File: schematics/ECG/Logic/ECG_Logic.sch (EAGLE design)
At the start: 77 parts, among them IC1 ADS1293, IC2 LIS3DH, IC3 MCP1703, IC4 CC2541, IC5 FSA4157, IC6 FSA4157, IC7 FSA4157, IC8 BALUN_2450BM_SERIES_SMD, X1 XTAL-2SMD, X2 XTAL_403, X3 ECS-40-20-4VX

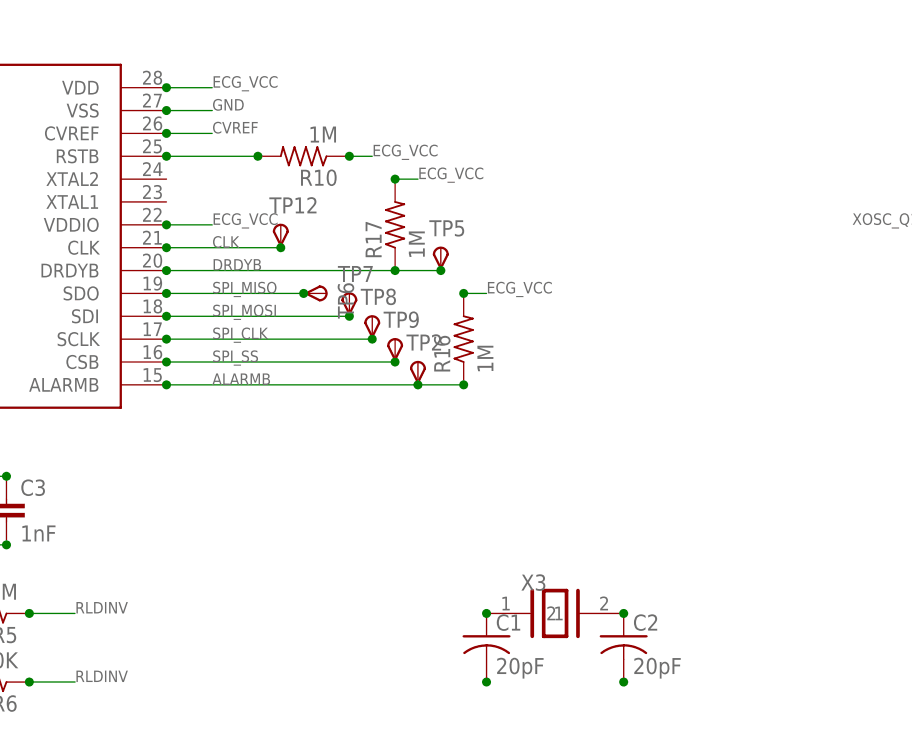
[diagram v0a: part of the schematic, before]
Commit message: expanded board size for new low profile crystal. Moved ecg input targets for shorter trace lengths to ADS1293
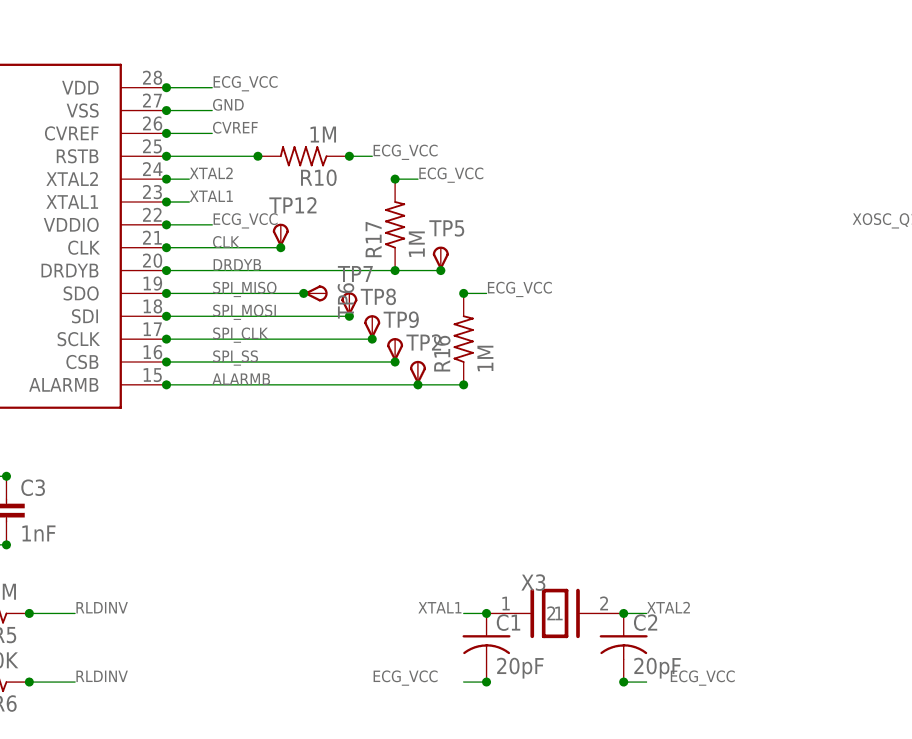
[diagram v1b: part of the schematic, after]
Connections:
- removed net N$1: C1.1, X3.1
- removed net N$10: C1.2
- removed net N$2: C2.1, X3.2
- removed net N$7: C2.2
- new net XTAL1: C1.1, IC1.XTAL1, X3.1
- new net XTAL2: C2.1, IC1.XTAL2, X3.2
- net ECG_VCC: now also C1.2, C2.2
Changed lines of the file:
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@@
 <grid distance="0.1" unitdist="inch" unit="inch" style="lines" multiple="1" display="no" altdistance="0.01" altunitdist="inch" altunit="inch"/>
 <layers>
-<layer number="1" name="Top" color="4" fill="1" visible="yes" active="no"/>
-<layer number="2" name="Route2" color="1" fill="3" visible="yes" active="no"/>
-<layer number="3" name="Route3" color="4" fill="3" visible="yes" active="no"/>
-<layer number="4" name="Route4" color="1" fill="4" visible="yes" active="no"/>
-<layer number="5" name="Route5" color="4" fill="4" visible="yes" active="no"/>
-<layer number="6" name="Route6" color="1" fill="8" visible="yes" active="no"/>
-<layer number="7" name="Route7" color="4" fill="8" visible="yes" active="no"/>
-<layer number="8" name="Route8" color="1" fill="2" visible="yes" active="no"/>
-<layer number="9" name="Route9" color="4" fill="2" visible="yes" active="no"/>
-<layer number="10" name="Route10" color="1" fill="7" visible="yes" active="no"/>
-<layer number="11" name="Route11" color="4" fill="7" visible="yes" active="no"/>
-<layer number="12" name="Route12" color="1" fill="5" visible="yes" active="no"/>
-<layer number="13" name="Route13" color="4" fill="5" visible="yes" active="no"/>
-<layer number="14" name="Route14" color="1" fill="6" visible="yes" active="no"/>
-<layer number="15" name="Route15" color="4" fill="6" visible="yes" active="no"/>
-<layer number="16" name="Bottom" color="1" fill="1" visible="yes" active="no"/>
-<layer number="17" name="Pads" color="2" fill="1" visible="yes" active="no"/>
-<layer number="18" name="Vias" color="2" fill="1" visible="yes" active="no"/>
-<layer number="19" name="Unrouted" color="6" fill="1" visible="yes" active="no"/>
-<layer number="20" name="Dimension" color="15" fill="1" visible="yes" active="no"/>
-<layer number="21" name="tPlace" color="7" fill="1" visible="yes" active="no"/>
-<layer number="22" name="bPlace" color="7" fill="1" visible="yes" active="no"/>
-<layer number="23" name="tOrigins" color="15" fill="1" visible="yes" active="no"/>
-<layer number="24" name="bOrigins" color="15" fill="1" visible="yes" active="no"/>
-<layer number="25" name="tNames" color="7" fill="1" visible="yes" active="no"/>
-<layer number="26" name="bNames" color="7" fill="1" visible="yes" active="no"/>
-<layer number="27" name="tValues" color="7" fill="1" visible="yes" active="no"/>
-<layer number="28" name="bValues" color="7" fill="1" visible="yes" active="no"/>
+<layer number="1" name="Top" color="4" fill="1" visible="no" active="no"/>
+<layer number="2" name="Route2" color="1" fill="3" visible="no" active="no"/>
+<layer number="3" name="Route3" color="4" fill="3" visible="no" active="no"/>
+<layer number="4" name="Route4" color="1" fill="4" visible="no" active="no"/>
+<layer number="5" name="Route5" color="4" fill="4" visible="no" active="no"/>
+<layer number="6" name="Route6" color="1" fill="8" visible="no" active="no"/>
+<layer number="7" name="Route7" color="4" fill="8" visible="no" active="no"/>
+<layer number="8" name="Route8" color="1" fill="2" visible="no" active="no"/>
+<layer number="9" name="Route9" color="4" fill="2" visible="no" active="no"/>
+<layer number="10" name="Route10" color="1" fill="7" visible="no" active="no"/>
+<layer number="11" name="Route11" color="4" fill="7" visible="no" active="no"/>
+<layer number="12" name="Route12" color="1" fill="5" visible="no" active="no"/>
+<layer number="13" name="Route13" color="4" fill="5" visible="no" active="no"/>
+<layer number="14" name="Route14" color="1" fill="6" visible="no" active="no"/>
+<layer number="15" name="Route15" color="4" fill="6" visible="no" active="no"/>
+<layer number="16" name="Bottom" color="1" fill="1" visible="no" active="no"/>
+<layer number="17" name="Pads" color="2" fill="1" visible="no" active="no"/>
+<layer number="18" name="Vias" color="2" fill="1" visible="no" active="no"/>
+<layer number="19" name="Unrouted" color="6" fill="1" visible="no" active="no"/>
+<layer number="20" name="Dimension" color="15" fill="1" visible="no" active="no"/>
+<layer number="21" name="tPlace" color="7" fill="1" visible="no" active="no"/>
+<layer number="22" name="bPlace" color="7" fill="1" visible="no" active="no"/>
+<layer number="23" name="tOrigins" color="15" fill="1" visible="no" active="no"/>
+<layer number="24" name="bOrigins" color="15" fill="1" visible="no" active="no"/>
+<layer number="25" name="tNames" color="7" fill="1" visible="no" active="no"/>
+<layer number="26" name="bNames" color="7" fill="1" visible="no" active="no"/>
+<layer number="27" name="tValues" color="7" fill="1" visible="no" active="no"/>
+<layer number="28" name="bValues" color="7" fill="1" visible="no" active="no"/>
 <layer number="29" name="tStop" color="7" fill="3" visible="no" active="no"/>
 <layer number="30" name="bStop" color="7" fill="6" visible="no" active="no"/>
@@
 <layer number="35" name="tGlue" color="7" fill="4" visible="no" active="no"/>
 <layer number="36" name="bGlue" color="7" fill="5" visible="no" active="no"/>
-<layer number="37" name="tTest" color="7" fill="1" visible="yes" active="no"/>
-<layer number="38" name="bTest" color="7" fill="1" visible="yes" active="no"/>
+<layer number="37" name="tTest" color="7" fill="1" visible="no" active="no"/>
+<layer number="38" name="bTest" color="7" fill="1" visible="no" active="no"/>
 <layer number="39" name="tKeepout" color="4" fill="11" visible="no" active="no"/>
 <layer number="40" name="bKeepout" color="1" fill="11" visible="no" active="no"/>
@@
 <layer number="44" name="Drills" color="7" fill="1" visible="no" active="no"/>
 <layer number="45" name="Holes" color="7" fill="1" visible="no" active="no"/>
-<layer number="46" name="Milling" color="3" fill="1" visible="yes" active="no"/>
-<layer number="47" name="Measures" color="7" fill="1" visible="yes" active="no"/>
-<layer number="48" name="Document" color="7" fill="1" visible="yes" active="no"/>
-<layer number="49" name="Reference" color="7" fill="1" visible="yes" active="no"/>
-<layer number="50" name="dxf" color="7" fill="1" visible="yes" active="no"/>
-<layer number="51" name="tDocu" color="7" fill="1" visible="yes" active="no"/>
-<layer number="52" name="bDocu" color="7" fill="1" visible="yes" active="no"/>
-<layer number="53" name="tGND_GNDA" color="7" fill="9" visible="yes" active="no"/>
-<layer number="54" name="bGND_GNDA" color="1" fill="9" visible="yes" active="no"/>
-<layer number="56" name="wert" color="7" fill="1" visible="yes" active="no"/>
+<layer number="46" name="Milling" color="3" fill="1" visible="no" active="no"/>
+<layer number="47" name="Measures" color="7" fill="1" visible="no" active="no"/>
+<layer number="48" name="Document" color="7" fill="1" visible="no" active="no"/>
+<layer number="49" name="Reference" color="7" fill="1" visible="no" active="no"/>
+<layer number="50" name="dxf" color="7" fill="1" visible="no" active="no"/>
+<layer number="51" name="tDocu" color="7" fill="1" visible="no" active="no"/>
+<layer number="52" name="bDocu" color="7" fill="1" visible="no" active="no"/>
+<layer number="53" name="tGND_GNDA" color="7" fill="9" visible="no" active="no"/>
+<layer number="54" name="bGND_GNDA" color="1" fill="9" visible="no" active="no"/>
+<layer number="56" name="wert" color="7" fill="1" visible="no" active="no"/>
 <layer number="91" name="Nets" color="2" fill="1" visible="yes" active="yes"/>
 <layer number="92" name="Busses" color="1" fill="1" visible="yes" active="yes"/>
@@
 <label x="114.3" y="66.04" size="1.27" layer="95"/>
 </segment>
+<segment>
+<pinref part="C1" gate="G$1" pin="2"/>
+<junction x="127" y="7.62"/>
+<wire x1="127" y1="7.62" x2="124.46" y2="7.62" width="0.1524" layer="91"/>
+<label x="114.3" y="7.62" size="1.27" layer="95"/>
+</segment>
+<segment>
+<pinref part="C2" gate="G$1" pin="2"/>
+<junction x="142.24" y="7.62"/>
+<wire x1="142.24" y1="7.62" x2="144.78" y2="7.62" width="0.1524" layer="91"/>
+<label x="147.32" y="7.62" size="1.27" layer="95"/>
+</segment>
 </net>
 <net name="BLUE_LED" class="0">
@@
 </segment>
 </net>
-<net name="N$1" class="0">
+<net name="XTAL1" class="0">
+<segment>
+<pinref part="IC1" gate="IC" pin="XTAL1"/>
+<wire x1="91.44" y1="60.96" x2="93.98" y2="60.96" width="0.1524" layer="91"/>
+<junction x="91.44" y="60.96"/>
+<label x="93.98" y="60.96" size="1.27" layer="95"/>
+</segment>
 <segment>
 <pinref part="X3" gate="XTAL" pin="1"/>
 <pinref part="C1" gate="G$1" pin="1"/>
 <junction x="127" y="15.24"/>
-</segment>
-</net>
-<net name="N$2" class="0">
+<wire x1="127" y1="15.24" x2="124.46" y2="15.24" width="0.1524" layer="91"/>
+<label x="119.38" y="15.24" size="1.27" layer="95"/>
+</segment>
+</net>
+<net name="XTAL2" class="0">
+<segment>
+<pinref part="IC1" gate="IC" pin="XTAL2"/>
+<wire x1="91.44" y1="63.5" x2="93.98" y2="63.5" width="0.1524" layer="91"/>
+<junction x="91.44" y="63.5"/>
+<label x="93.98" y="63.5" size="1.27" layer="95"/>
+</segment>
 <segment>
 <pinref part="X3" gate="XTAL" pin="2"/>
 <pinref part="C2" gate="G$1" pin="1"/>
 <junction x="142.24" y="15.24"/>
-</segment>
-</net>
-<net name="N$7" class="0">
-<segment>
-<pinref part="C2" gate="G$1" pin="2"/>
-<junction x="142.24" y="7.62"/>
-</segment>
-</net>
-<net name="N$10" class="0">
-<segment>
-<pinref part="C1" gate="G$1" pin="2"/>
-<junction x="127" y="7.62"/>
-</segment>
-</net>
+<wire x1="142.24" y1="15.24" x2="144.78" y2="15.24" width="0.1524" layer="91"/>
+<label x="144.78" y="15.24" size="1.27" layer="95"/>
+</segment>
+</net>

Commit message: updated all boards to slightly larger dimensions and new target/piston positions
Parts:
- renumbered U$1 to P1, U$2 to P2, U$3 to P3, U$4 to P4, U$5 to P5, U$6 to P6, U$7 to P7
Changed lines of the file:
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@@
 <part name="TP1" library="testpad" deviceset="TPS" device="TP08SQ"/>
 <part name="TP2" library="testpad" deviceset="TPS" device="TP06R" value="TPSTP06R"/>
-<part name="U$1" library="pins" deviceset="TARGET_RA" device=""/>
-<part name="U$2" library="pins" deviceset="TARGET_RA" device=""/>
-<part name="U$3" library="pins" deviceset="TARGET_RA" device=""/>
-<part name="U$4" library="pins" deviceset="TARGET_RA" device=""/>
-<part name="U$5" library="pins" deviceset="TARGET_RA" device=""/>
-<part name="U$6" library="pins" deviceset="TARGET_RA" device=""/>
-<part name="U$7" library="pins" deviceset="TARGET_RA" device=""/>
+<part name="P1" library="pins" deviceset="TARGET_RA" device=""/>
+<part name="P2" library="pins" deviceset="TARGET_RA" device=""/>
+<part name="P3" library="pins" deviceset="TARGET_RA" device=""/>
+<part name="P4" library="pins" deviceset="TARGET_RA" device=""/>
+<part name="P5" library="pins" deviceset="TARGET_RA" device=""/>
+<part name="P6" library="pins" deviceset="TARGET_RA" device=""/>
+<part name="P7" library="pins" deviceset="TARGET_RA" device=""/>
 <part name="X3" library="ecs" deviceset="ECS-40-20-4VX" device=""/>
 <part name="C1" library="rcl" deviceset="C-US" device="C0201" value="20pF"/>
@@
 <instance part="TP1" gate="G$1" x="96.52" y="119.38"/>
 <instance part="TP2" gate="G$1" x="119.38" y="43.18"/>
-<instance part="U$1" gate="PIN" x="187.96" y="200.66"/>
-<instance part="U$2" gate="PIN" x="187.96" y="198.12"/>
-<instance part="U$3" gate="PIN" x="187.96" y="203.2"/>
-<instance part="U$4" gate="PIN" x="187.96" y="205.74"/>
-<instance part="U$5" gate="PIN" x="187.96" y="195.58"/>
-<instance part="U$6" gate="PIN" x="187.96" y="193.04"/>
-<instance part="U$7" gate="PIN" x="187.96" y="187.96"/>
+<instance part="P1" gate="PIN" x="187.96" y="200.66"/>
+<instance part="P2" gate="PIN" x="187.96" y="198.12"/>
+<instance part="P3" gate="PIN" x="187.96" y="203.2"/>
+<instance part="P4" gate="PIN" x="187.96" y="205.74"/>
+<instance part="P5" gate="PIN" x="187.96" y="195.58"/>
+<instance part="P6" gate="PIN" x="187.96" y="193.04"/>
+<instance part="P7" gate="PIN" x="187.96" y="187.96"/>
 <instance part="X3" gate="XTAL" x="134.62" y="15.24"/>
 <instance part="C1" gate="G$1" x="127" y="12.7"/>
@@
 </segment>
 <segment>
-<pinref part="U$5" gate="PIN" pin="1"/>
+<pinref part="P5" gate="PIN" pin="1"/>
 <wire x1="182.88" y1="195.58" x2="180.34" y2="195.58" width="0.1524" layer="91"/>
 <junction x="182.88" y="195.58"/>
@@
 </segment>
 <segment>
-<pinref part="U$3" gate="PIN" pin="1"/>
+<pinref part="P3" gate="PIN" pin="1"/>
 <wire x1="182.88" y1="203.2" x2="180.34" y2="203.2" width="0.1524" layer="91"/>
 <junction x="182.88" y="203.2"/>
@@
 </segment>
 <segment>
-<pinref part="U$1" gate="PIN" pin="1"/>
+<pinref part="P1" gate="PIN" pin="1"/>
 <wire x1="182.88" y1="200.66" x2="180.34" y2="200.66" width="0.1524" layer="91"/>
 <junction x="182.88" y="200.66"/>
@@
 </segment>
 <segment>
-<pinref part="U$4" gate="PIN" pin="1"/>
+<pinref part="P4" gate="PIN" pin="1"/>
 <wire x1="182.88" y1="205.74" x2="180.34" y2="205.74" width="0.1524" layer="91"/>
 <junction x="182.88" y="205.74"/>
@@
 </segment>
 <segment>
-<pinref part="U$2" gate="PIN" pin="1"/>
+<pinref part="P2" gate="PIN" pin="1"/>
 <wire x1="182.88" y1="198.12" x2="180.34" y2="198.12" width="0.1524" layer="91"/>
 <junction x="182.88" y="198.12"/>
@@
 </segment>
 <segment>
-<pinref part="U$6" gate="PIN" pin="1"/>
+<pinref part="P6" gate="PIN" pin="1"/>
 <wire x1="182.88" y1="193.04" x2="180.34" y2="193.04" width="0.1524" layer="91"/>
 <junction x="182.88" y="193.04"/>
@@
 <net name="BOARD_DETECT" class="0">
 <segment>
-<pinref part="U$7" gate="PIN" pin="1"/>
+<pinref part="P7" gate="PIN" pin="1"/>
 <wire x1="182.88" y1="187.96" x2="180.34" y2="187.96" width="0.1524" layer="91"/>
 <junction x="182.88" y="187.96"/>

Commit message: board only gets power when external accessory is plugged into it
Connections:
- removed net BOARD_DETECT: IC4.SCL, P7.1
- new net BATT_DETECT: C4.1, IC3.VIN, IC5.B1, P7.1
- net BATT: no longer C4.1, IC3.VIN, IC5.B1
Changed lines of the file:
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@@
 <?xml version="1.0" encoding="utf-8"?>
 <!DOCTYPE eagle SYSTEM "eagle.dtd">
-<eagle version="6.5.0">
+<eagle version="6.4">
 <drawing>
 <settings>
@@
 <net name="BATT" class="0">
 <segment>
-<pinref part="IC5" gate="FSA4157" pin="B1"/>
-<junction x="76.2" y="205.74"/>
-<wire x1="76.2" y1="205.74" x2="71.12" y2="205.74" width="0.1524" layer="91"/>
-<label x="68.58" y="205.74" size="1.778" layer="95"/>
-</segment>
-<segment>
-<pinref part="IC3" gate="IC" pin="VIN"/>
-<junction x="152.4" y="180.34"/>
-<wire x1="152.4" y1="180.34" x2="147.32" y2="180.34" width="0.1524" layer="91"/>
-<pinref part="C4" gate="G$1" pin="1"/>
-<wire x1="147.32" y1="180.34" x2="144.78" y2="180.34" width="0.1524" layer="91"/>
-<junction x="147.32" y="180.34"/>
-<label x="139.7" y="180.34" size="1.27" layer="95"/>
-</segment>
-<segment>
 <pinref part="P6" gate="PIN" pin="1"/>
 <wire x1="182.88" y1="193.04" x2="180.34" y2="193.04" width="0.1524" layer="91"/>
@@
 </segment>
 </net>
-<net name="BOARD_DETECT" class="0">
-<segment>
-<pinref part="P7" gate="PIN" pin="1"/>
-<wire x1="182.88" y1="187.96" x2="180.34" y2="187.96" width="0.1524" layer="91"/>
-<junction x="182.88" y="187.96"/>
-<label x="165.1" y="187.96" size="1.27" layer="95"/>
-</segment>
-<segment>
-<pinref part="IC4" gate="G$1" pin="SCL"/>
-<wire x1="205.74" y1="78.74" x2="203.2" y2="78.74" width="0.1524" layer="91"/>
-<junction x="205.74" y="78.74"/>
-<label x="190.5" y="78.74" size="1.27" layer="95"/>
-</segment>
-</net>
 <net name="XTAL1" class="0">
 <segment>
@@
 </segment>
 </net>
+<net name="BATT_DETECT" class="0">
+<segment>
+<pinref part="IC3" gate="IC" pin="VIN"/>
+<junction x="152.4" y="180.34"/>
+<wire x1="152.4" y1="180.34" x2="147.32" y2="180.34" width="0.1524" layer="91"/>
+<pinref part="C4" gate="G$1" pin="1"/>
+<wire x1="147.32" y1="180.34" x2="144.78" y2="180.34" width="0.1524" layer="91"/>
+<junction x="147.32" y="180.34"/>
+<label x="134.62" y="180.34" size="1.27" layer="95"/>
+</segment>
+<segment>
+<pinref part="IC5" gate="FSA4157" pin="B1"/>
+<junction x="76.2" y="205.74"/>
+<wire x1="76.2" y1="205.74" x2="71.12" y2="205.74" width="0.1524" layer="91"/>
+<label x="60.96" y="205.74" size="1.27" layer="95"/>
+</segment>
+<segment>
+<pinref part="P7" gate="PIN" pin="1"/>
+<wire x1="182.88" y1="187.96" x2="180.34" y2="187.96" width="0.1524" layer="91"/>
+<junction x="182.88" y="187.96"/>
+<label x="167.64" y="187.96" size="1.27" layer="95"/>
+</segment>
+</net>

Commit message: added 47uF cap to battery
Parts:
- added C27: (no value), rcl:C-USC0805
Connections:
- net BATT_DETECT: now also C27.1
- net GND: now also C27.2
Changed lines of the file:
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@@
 <?xml version="1.0" encoding="utf-8"?>
 <!DOCTYPE eagle SYSTEM "eagle.dtd">
-<eagle version="6.4">
+<eagle version="6.5.0">
 <drawing>
 <settings>
@@
 <part name="C1" library="rcl" deviceset="C-US" device="C0201" value="20pF"/>
 <part name="C2" library="rcl" deviceset="C-US" device="C0201" value="20pF"/>
+<part name="C27" library="rcl" deviceset="C-US" device="C0805"/>
+<part name="GND17" library="supply1" deviceset="GND" device=""/>
 </parts>
 <sheets>
@@
 <instance part="C1" gate="G$1" x="127" y="12.7"/>
 <instance part="C2" gate="G$1" x="142.24" y="12.7"/>
+<instance part="C27" gate="G$1" x="182.88" y="185.42"/>
+<instance part="GND17" gate="1" x="182.88" y="177.8" rot="MR0"/>
 </instances>
 <busses>
@@
 <junction x="182.88" y="195.58"/>
 <label x="175.26" y="195.58" size="1.27" layer="95"/>
+</segment>
+<segment>
+<pinref part="C27" gate="G$1" pin="2"/>
+<pinref part="GND17" gate="1" pin="GND"/>
+<junction x="182.88" y="180.34"/>
 </segment>
 </net>
@@
 <junction x="182.88" y="187.96"/>
 <label x="167.64" y="187.96" size="1.27" layer="95"/>
-</segment>
-</net>
+<pinref part="C27" gate="G$1" pin="1"/>
+</segment>
+</net>

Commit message: removed board comments that are no long applicable. Added missing values to scheamtic components
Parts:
- C27: value (none) -> 47uF
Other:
- note removed: "add 47uF cap to batt+"
- note removed: "add batt/gnd pads"
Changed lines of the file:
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@@
 <part name="C1" library="rcl" deviceset="C-US" device="C0201" value="20pF"/>
 <part name="C2" library="rcl" deviceset="C-US" device="C0201" value="20pF"/>
-<part name="C27" library="rcl" deviceset="C-US" device="C0805"/>
+<part name="C27" library="rcl" deviceset="C-US" device="C0805" value="47uF"/>
 <part name="GND17" library="supply1" deviceset="GND" device=""/>
 </parts>
@@
 <text x="182.88" y="40.64" size="1.27" layer="95">32MHz</text>
 <text x="236.22" y="40.64" size="1.27" layer="95">32.768KHz</text>
-<text x="2.54" y="228.6" size="1.778" layer="91">add 47uF cap to batt+</text>
-<text x="2.54" y="226.06" size="1.778" layer="91">add batt/gnd pads</text>
 </plain>
 <instances>

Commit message: removed unused scheamtic trace, updated BOM
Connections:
- removed net OSC_SW_VCC: IC4.SDA
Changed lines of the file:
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@@
 <?xml version="1.0" encoding="utf-8"?>
 <!DOCTYPE eagle SYSTEM "eagle.dtd">
-<eagle version="6.5.0">
+<eagle version="6.4">
 <drawing>
 <settings>
@@
 </segment>
 </net>
-<net name="OSC_SW_VCC" class="0">
-<segment>
-<pinref part="IC4" gate="G$1" pin="SDA"/>
-<wire x1="205.74" y1="76.2" x2="203.2" y2="76.2" width="0.1524" layer="91"/>
-<junction x="205.74" y="76.2"/>
-<label x="190.5" y="76.2" size="1.27" layer="95"/>
-</segment>
-</net>
